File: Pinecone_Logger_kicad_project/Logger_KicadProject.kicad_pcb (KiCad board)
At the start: 4 copper layers, 63.5 x 52.3 mm, 50 parts, among them J1 PJ-102A, J2 M50-3600542, J3 DM3AT-SF-PEJM5, J4 OSTVN06A150, J5 OSTVN06A150, J6 OSTVN06A150, J7 OSTVN06A150, J8 10_Pin_Header, Q1 AO3420, Q2 AO3420, Q3 AO3420, Q4 AO3420, U1 SAMD20E16A-A, U2 MIC5211, U3 AP2281, U4 DS1302, U5 MAX4618, U6 MAX31856, Y1 CFS-20632768EZBB

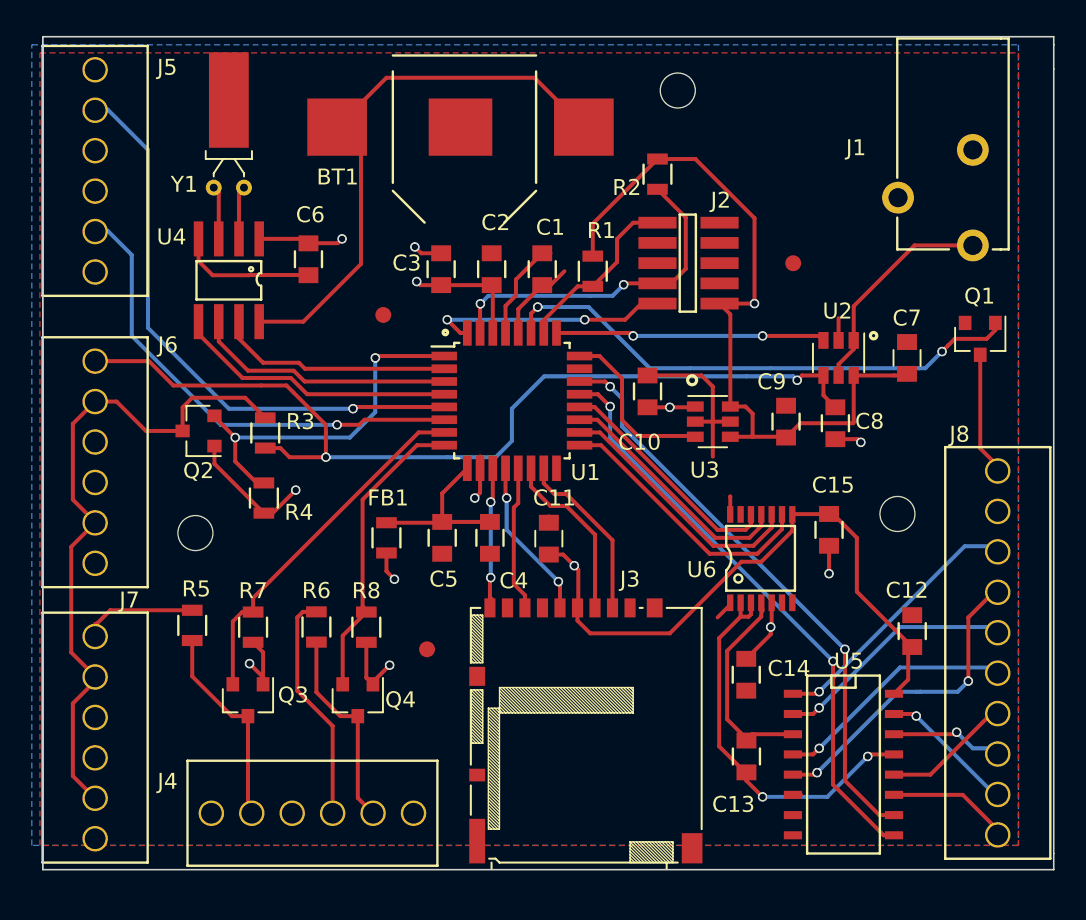
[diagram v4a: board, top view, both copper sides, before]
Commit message: added MAX3231 to board, changed xlator mosfets to work
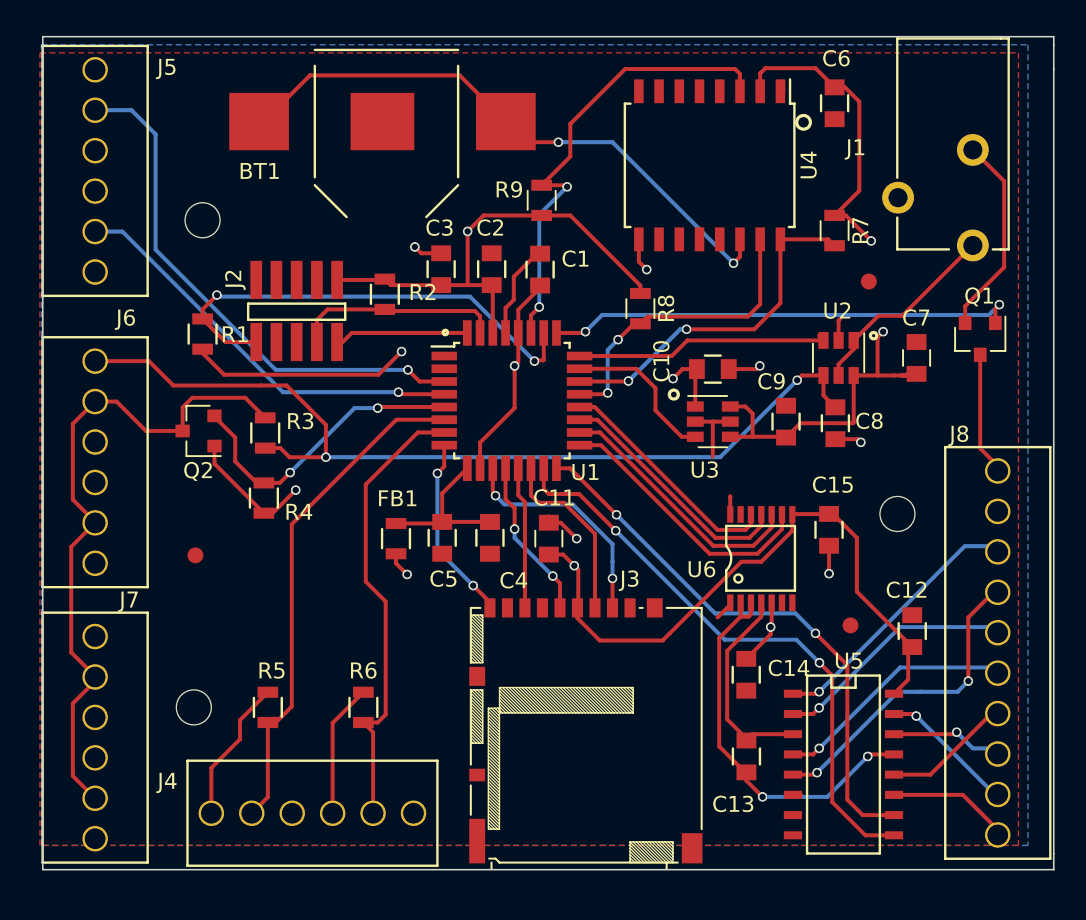
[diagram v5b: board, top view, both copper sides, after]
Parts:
- removed Q3, Q4: AO3420, TO_SOT_Packages_SMD:SOT-23
- removed Y1: CFS-20632768EZBB, Crystals:Crystal_DS26_d2.0mm_l6.0mm_Horizontal_1EP_style1
- added R9: RC0805JR-0710KL, Resistors_SMD:R_0805, F.Cu at (45.0, 43.3)
- C10, C11, C12, C13, C14, C15, C2, C5, C6, C7, C8: value CC0603ZRY5V9BB104 -> C0805C104K5RACTU
- U4: value DS1302 -> DS3231; footprint Pinecone_footprints:SOIC-8 -> Housings_SOIC:SOIC-16W_7.5x10.3mm_Pitch1.27mm
- moved R7 44.2 mm to (63.5, 45.2), turned to 270 degrees
- moved FID1 41.8 mm to (23.3, 65.6)
- moved C6 34.5 mm to (63.5, 37.2)
- moved REF** 30.9 mm to (23.8, 44.5)
- moved FID2 30.6 mm to (65.6, 48.4)
- moved U4 28.7 mm to (55.6, 41.1)
- moved FID3 26.6 mm to (64.5, 70.0)
- moved R8 26.4 mm to (51.2, 50.1), turned to 270 degrees
- moved R1 24.8 mm to (23.8, 51.7), turned to 90 degrees
- moved J2 20.3 mm to (32.2, 52.2), turned to 180 degrees
- moved R2 18.7 mm to (35.2, 49.2)
- moved REF** 11.0 mm to (23.2, 75.2)
- moved R5 7.01 mm to (27.9, 75.2)
- moved R6 5.85 mm to (33.9, 75.2)
- moved BT1 4.91 mm to (42.8, 38.4)
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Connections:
- J3 pad M1: (no net) -> Net-(J3-PadM1)
- J4 pad 1: SWITCHED_5v -> SWITCHED_3v3
- J4 pad 2: Net-(J4-Pad2) -> DHT22_1
- J4 pad 4: SWITCHED_5v -> SWITCHED_3v3
- J4 pad 5: Net-(J4-Pad5) -> DHT22_2
- R5 pad 1: SWITCHED_5v -> SWITCHED_3v3
- R5 pad 2: Net-(J4-Pad2) -> DHT22_1
- R6 pad 1: SWITCHED_5v -> SWITCHED_3v3
- R6 pad 2: Net-(J4-Pad5) -> DHT22_2
- R7 pad 1: SWITCHED_3v3 -> +3V3
- R7 pad 2: DHT22_1 -> DS3231_SCL
- R8 pad 1: SWITCHED_3v3 -> +3V3
- R8 pad 2: DHT22_2 -> DS3231_SDA
- U1 pad 1: SDI_3v3_DATA -> Net-(U1-Pad1)
- U1 pad 11: SD_CHIP_DETECT -> SD_SERCOM_PAD1_CS
- U1 pad 15: SD_SERCOM_PAD1_CS -> MUX_SEL_B
- U1 pad 16: Net-(U1-Pad16) -> MUX_SEL_A
- U1 pad 2: DS1302_SCLK -> Net-(U1-Pad2)
- U1 pad 21: MUX_SEL_B -> DS3231_SDA
- U1 pad 22: MUX_SEL_A -> DS3231_SCL
- U1 pad 23: Net-(U1-Pad23) -> 3v3_PWR_ENABLE
- U1 pad 24: 3v3_PWR_ENABLE -> 5v_PWR_ENABLE
- U1 pad 25: 5v_PWR_ENABLE -> HEATER_ENABLE
- U1 pad 27: HEATER_ENABLE -> DS3231_INTERRUPT
- U1 pad 3: DS1302_IO -> Dend1
- U1 pad 4: DS1302_CE -> Dend2
- U1 pad 5: Dend1 -> SDI_3v3_DATA
- U1 pad 6: Dend2 -> DHT22_1
- U1 pad 7: DHT22_1 -> DHT22_2
- U1 pad 8: DHT22_2 -> SD_CHIP_DETECT
- U4 pad 1: +3V3 -> Net-(U4-Pad1)
- U4 pad 2: Net-(U4-Pad2) -> +3V3
- U4 pad 3: Net-(U4-Pad3) -> DS3231_INTERRUPT
- U4 pad 4: GND -> Net-(U4-Pad4)
- U4 pad 5: DS1302_CE -> GND
- U4 pad 6: DS1302_IO -> GND
- U4 pad 7: DS1302_SCLK -> GND
- U4 pad 8: Net-(BT1-Pad1) -> GND
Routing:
- net DS3231_INTERRUPT: track 0.00 -> 29.7 mm, vias 0 -> 2
- net +3V3: track 63.3 -> 86.3 mm, vias 4 -> 5
- net SWITCHED_5v: track 80.4 -> 57.9 mm
- net DS3231_SCL: track 0.00 -> 22.2 mm, vias 0 -> 2
- net DS3231_SDA: track 0.00 -> 19.3 mm, vias 0 -> 2
- net RESET: track 11.3 -> 29.8 mm, vias 0 -> 2
- net DS1302_CE: track 17.8 -> 0.00 mm
- net DS1302_IO: track 16.5 -> 0.00 mm
- net DS1302_SCLK: track 14.8 -> 0.00 mm
- net Net-(J4-Pad2): track 13.0 -> 0.00 mm
- net Net-(J4-Pad5): track 12.9 -> 0.00 mm
- net DHT22_2: track 18.9 -> 28.8 mm
- net GND: track 39.1 -> 48.3 mm, vias 4 -> 7
- net SWITCHED_3v3: track 64.2 -> 73.4 mm, vias 6 -> 4
- net DHT22_1: track 23.2 -> 31.8 mm
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
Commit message: Finished Logger V2 design, ready for pcb order
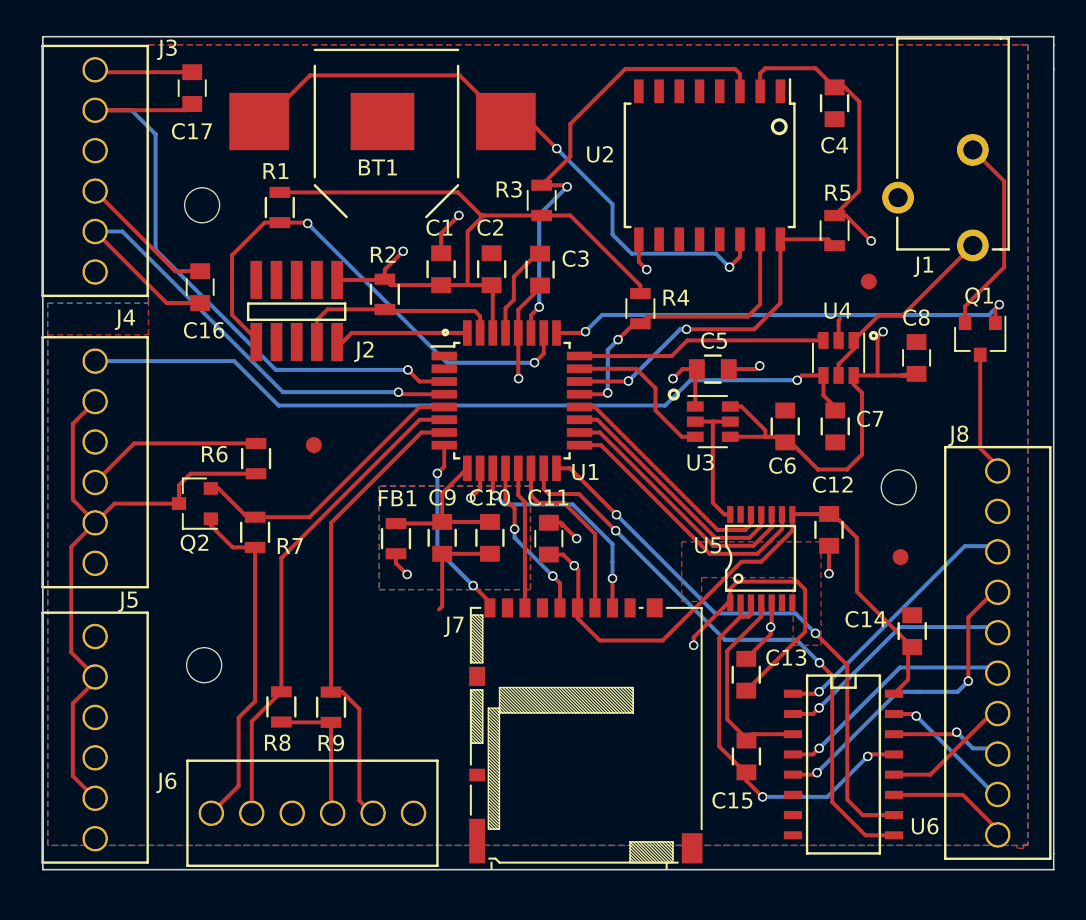
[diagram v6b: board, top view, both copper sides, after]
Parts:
- added C16: C0805C104K5RACTU, Capacitors_SMD:C_0805, F.Cu at (23.6, 48.8)
- added C17: C0805C104K5RACTU, Capacitors_SMD:C_0805, F.Cu at (23.1, 36.2)
- moved FID1 10.2 mm to (30.7, 58.7)
- moved R1 9.31 mm to (28.6, 43.8), turned to 270 degrees
- moved FID3 5.32 mm to (67.6, 65.7)
- moved Q2 4.57 mm to (23.3, 62.4)
- moved REF** 2.73 mm to (23.9, 72.5)
- moved R7 2.22 mm to (27.1, 64.2)
- moved R9 2.03 mm to (31.8, 75.1), turned to 90 degrees
- moved R6 1.71 mm to (27.1, 59.5), turned to 270 degrees
- moved REF** 1.67 mm to (67.5, 61.3)
- moved REF** 0.94 mm to (23.7, 43.6)
- moved R8 0.85 mm to (28.7, 75.1), turned to 90 degrees
- moved C6 0.30 mm to (60.4, 57.5)
- moved C7 0.20 mm to (63.5, 57.5)
- renumbered C3 to C1, C4 to C10, C15 to C12, C14 to C13, C12 to C14, C13 to C15, C1 to C3, C6 to C4, C10 to C5, C9 to C6, C8 to C7, C7 to C8, C5 to C9, J5 to J3, J6 to J4, J7 to J5, J4 to J6, J3 to J7, R9 to R3, R8 to R4, R7 to R5, R3 to R6, R4 to R7, R5 to R8, R6 to R9, U4 to U2, U2 to U4, U6 to U5, U5 to U6
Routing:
- net GND: track 48.3 -> 68.9 mm, vias 7 -> 8
- net SWITCHED_3v3: track 73.4 -> 93.4 mm, vias 4 -> 3
- net Dend2: track 26.2 -> 34.6 mm
- net Dend1: track 33.2 -> 39.5 mm
- net +3V3: track 86.3 -> 92.4 mm, vias 5 -> 4
- net SWITCHED_5v: track 57.9 -> 61.1 mm, vias 2 -> 1
- net Net-(BT1-Pad1): track 37.6 -> 40.7 mm
- net RESET: track 29.8 -> 32.1 mm
- net Net-(J4-Pad2): track 42.2 -> 40.5 mm
- net DHT22_1: track 31.8 -> 30.6 mm
- net DHT22_2: track 28.8 -> 29.8 mm
- net SDI_3v3_DATA: track 19.1 -> 18.3 mm, vias 2 -> 0

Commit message: logger circuit design finished, and ordered
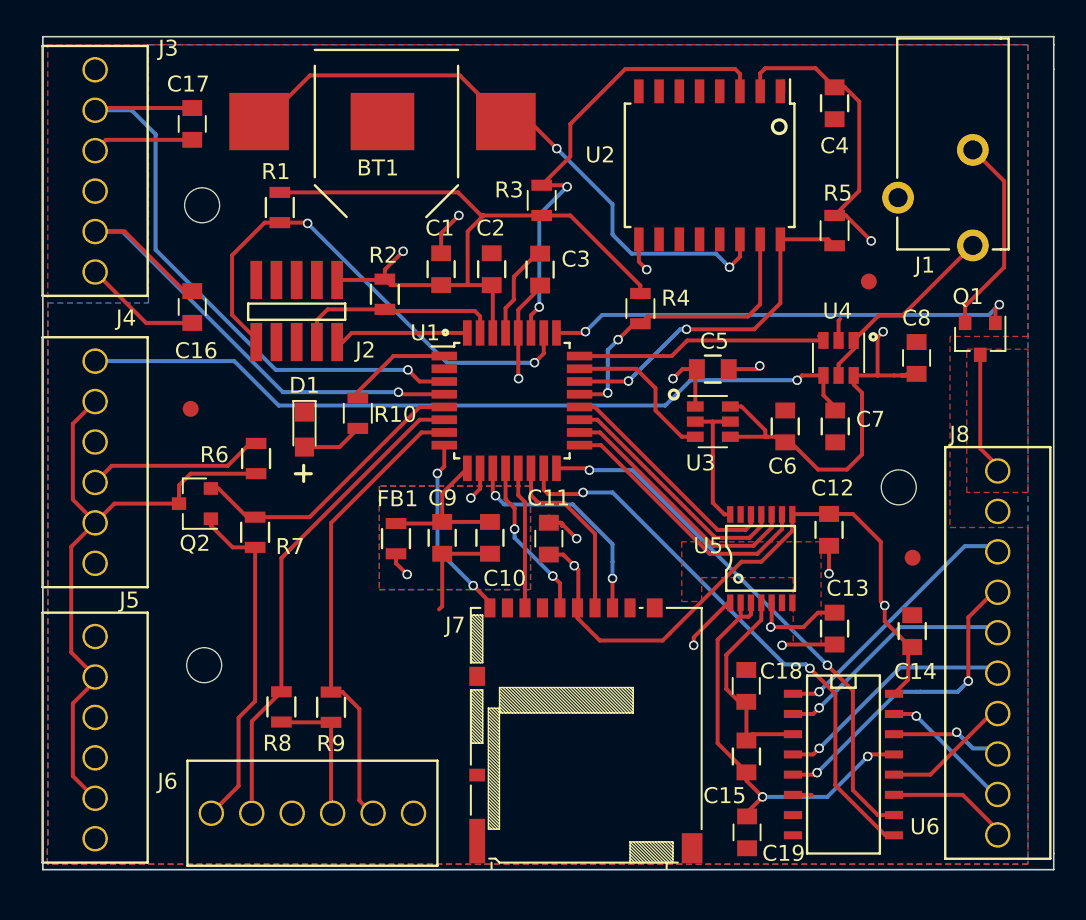
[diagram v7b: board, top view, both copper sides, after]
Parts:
- added C18: C0805C103K5RACTU, Capacitors_SMD:C_0805, F.Cu at (57.9, 73.8)
- added C19: C0805C103K5RACTU, Capacitors_SMD:C_0805, F.Cu at (58.0, 83.0)
- added D1: LY R976-PS-36, LEDs:LED_0805, F.Cu at (30.1, 57.7)
- added R10: RC0805JR-0768RL, Resistors_SMD:R_0805, F.Cu at (33.5, 56.7)
- moved FID1 8.07 mm to (23.0, 56.4)
- moved C13 6.26 mm to (63.5, 70.2)
- moved C17 2.25 mm to (23.1, 38.5)
- moved C16 1.35 mm to (23.1, 50.0)
- moved FID3 0.76 mm to (68.3, 65.8)
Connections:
- C16 pad 1: SWITCHED_3v3 -> Dend2
- C16 pad 2: Dend2 -> GND
- C17 pad 1: SWITCHED_3v3 -> Dend1
- C17 pad 2: Dend1 -> GND
- U1 pad 1: Net-(U1-Pad1) -> STATUS_LED
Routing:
- net SWITCHED_3v3: track 93.4 -> 81.9 mm, vias 3 -> 4
- net STATUS_LED: track 0.00 -> 6.76 mm
- net GND: track 68.9 -> 74.3 mm, vias 8 -> 9
- net Net-(D1-Pad2): track 0.00 -> 3.88 mm
- net Net-(C15-Pad2): track 24.7 -> 26.5 mm
- net MUX_SEL_A: track 35.6 -> 34.4 mm
- net MUX_SEL_B: track 37.0 -> 35.8 mm
- net Dend2: track 34.6 -> 34.1 mm
- added copper zone on F.Cu, net HEATER_SWITCHED_GND
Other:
- rule trace_min: 0.25 -> 0.01

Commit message: updated schematic and pcb to correctly use SAM D20 E18, not the E16
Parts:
- U1: value SAMD20E16A-A -> SAMD20E18A-A
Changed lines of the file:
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@@
     (links 157)
     (no_connects 0)
-    (area 13.665999 32.969999 77.266001 85.394001)
+    (area -3.857142 29.282142 85.363096 90.917857)
     (thickness 1.6)
     (drawings 30)
@@
       (effects (font (size 1 1) (thickness 0.15)))
     )
-    (fp_text value SAMD20E16A-A (at 0 6.05) (layer F.Fab)
+    (fp_text value SAMD20E18A-A (at 0 6.05) (layer F.Fab)
       (effects (font (size 1 1) (thickness 0.15)))
     )
@@
   (segment (start 39.9 35.45) (end 42.8 38.35) (width 0.25) (layer F.Cu) (net 1))
   (segment (start 44.1 39.65) (end 42.8 38.35) (width 0.25) (layer F.Cu) (net 1))
-  (segment (start 23.1 51) (end 20.2 51) (width 0.25) (layer F.Cu) (net 2) (status 400000))
-  (segment (start 20.2 51) (end 17 47.8) (width 0.25) (layer F.Cu) (net 2) (status 800000))
-  (segment (start 23.1 39.5) (end 17.68 39.5) (width 0.25) (layer F.Cu) (net 2) (status 400000))
-  (segment (start 17.68 39.5) (end 17 40.18) (width 0.25) (layer F.Cu) (net 2) (status 800000))
+  (segment (start 23.1 51) (end 20.2 51) (width 0.25) (layer F.Cu) (net 2))
+  (segment (start 20.2 51) (end 17 47.8) (width 0.25) (layer F.Cu) (net 2))
+  (segment (start 23.1 39.5) (end 17.68 39.5) (width 0.25) (layer F.Cu) (net 2))
+  (segment (start 17.68 39.5) (end 17 40.18) (width 0.25) (layer F.Cu) (net 2))
   (segment (start 57.95 84) (end 57.65 84) (width 0.25) (layer F.Cu) (net 2))
   (segment (start 60.833 80.645) (end 61.985 80.645) (width 0.25) (layer F.Cu) (net 2))
@@
   (segment (start 38.93 60.02) (end 38.93 58.68) (width 0.25) (layer F.Cu) (net 19))
   (segment (start 38.93 58.68) (end 38.32 58.68) (width 0.25) (layer F.Cu) (net 19))
-  (segment (start 23.1 49) (end 22.6 49) (width 0.25) (layer F.Cu) (net 20) (status C00000))
-  (segment (start 22.6 49) (end 18.86 45.26) (width 0.25) (layer F.Cu) (net 20) (status 400000))
-  (segment (start 18.86 45.26) (end 17 45.26) (width 0.25) (layer F.Cu) (net 20) (status 800000))
+  (segment (start 23.1 49) (end 22.6 49) (width 0.25) (layer F.Cu) (net 20))
+  (segment (start 22.6 49) (end 18.86 45.26) (width 0.25) (layer F.Cu) (net 20))
+  (segment (start 18.86 45.26) (end 17 45.26) (width 0.25) (layer F.Cu) (net 20))
   (segment (start 23.1 49) (end 23.1 48.82) (width 0.25) (layer F.Cu) (net 20))
   (segment (start 17 45.26) (end 17.11 45.26) (width 0.25) (layer F.Cu) (net 20))
@@
   (segment (start 28.8 55.35) (end 36.05 55.35) (width 0.25) (layer B.Cu) (net 20))
   (segment (start 18.71 45.26) (end 28.8 55.35) (width 0.25) (layer B.Cu) (net 20))
-  (segment (start 23.1 37.5) (end 17.14 37.5) (width 0.25) (layer F.Cu) (net 21) (status C00000))
-  (segment (start 17.14 37.5) (end 17 37.64) (width 0.25) (layer F.Cu) (net 21) (status C00000))
+  (segment (start 23.1 37.5) (end 17.14 37.5) (width 0.25) (layer F.Cu) (net 21))
+  (segment (start 17.14 37.5) (end 17 37.64) (width 0.25) (layer F.Cu) (net 21))
   (segment (start 22.71 37.64) (end 23.1 37.25) (width 0.25) (layer F.Cu) (net 21))
   (segment (start 17 37.64) (end 19.29 37.64) (width 0.25) (layer B.Cu) (net 21))
